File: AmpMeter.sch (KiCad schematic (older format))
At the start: 49 parts, among them J1 Vin L1-L3, J2 Serial, J3 ct1, J4 ct2, J5 ct3, J6 ct L1-L3, T1 Transformer_1P_1S, T2 Transformer_1P_1S, T3 Transformer_1P_1S, U1 LTV-817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

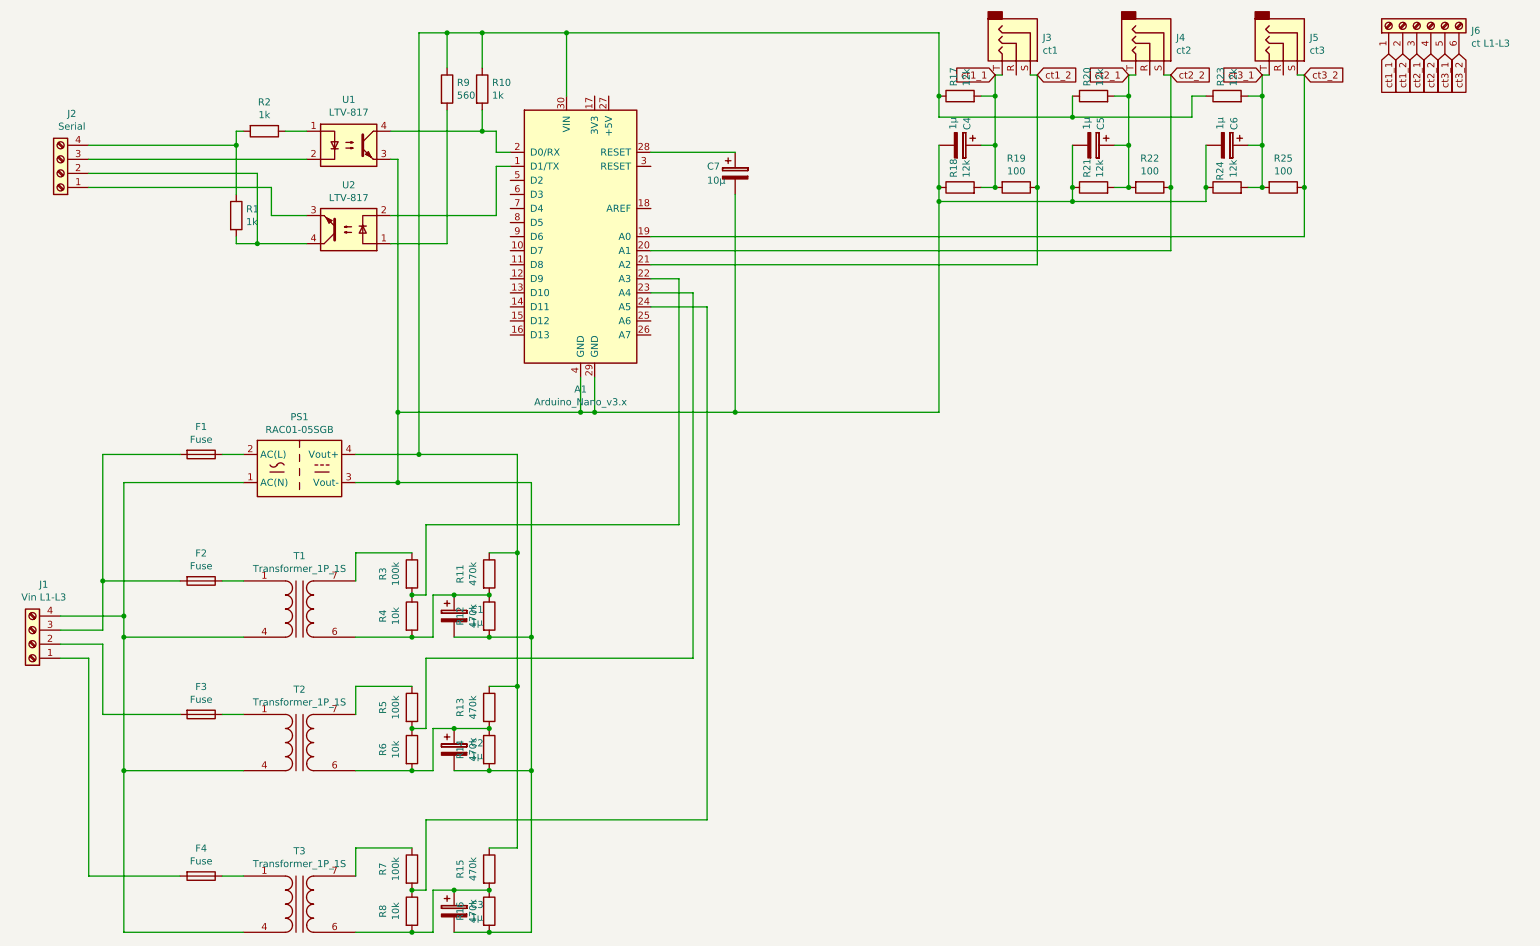
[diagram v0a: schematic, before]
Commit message: change values on parts
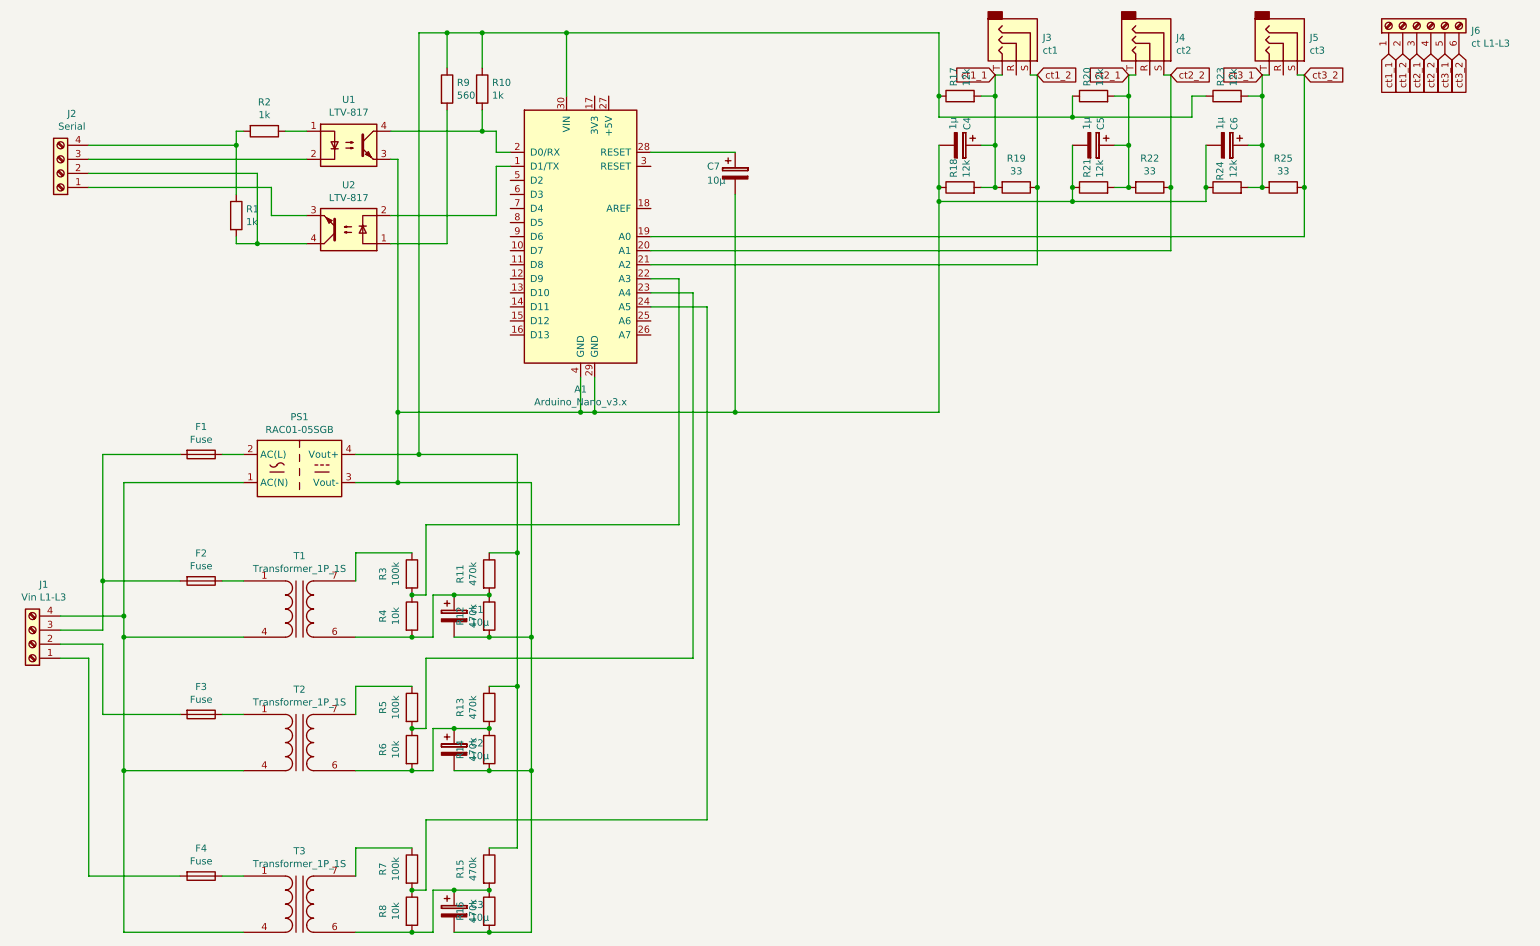
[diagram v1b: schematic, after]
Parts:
- C1, C2, C3: value 1µ -> 10µ
- R19, R22, R25: value 100 -> 33
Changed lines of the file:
@@
 P 7650 1950
 F 0 "R19" V 7443 1950 50  0000 C CNN
-F 1 "100" V 7534 1950 50  0000 C CNN
+F 1 "33" V 7534 1950 50  0000 C CNN
 F 2 "Resistor_SMD:R_1206_3216Metric" V 7580 1950 50  0001 C CNN
 F 3 "~" H 7650 1950 50  0001 C CNN
@@
 P 8600 1950
 F 0 "R22" V 8393 1950 50  0000 C CNN
-F 1 "100" V 8484 1950 50  0000 C CNN
+F 1 "33" V 8484 1950 50  0000 C CNN
 F 2 "Resistor_SMD:R_1206_3216Metric" V 8530 1950 50  0001 C CNN
 F 3 "~" H 8600 1950 50  0001 C CNN
@@
 P 9550 1950
 F 0 "R25" V 9343 1950 50  0000 C CNN
-F 1 "100" V 9434 1950 50  0000 C CNN
+F 1 "33" V 9434 1950 50  0000 C CNN
 F 2 "Resistor_SMD:R_1206_3216Metric" V 9480 1950 50  0001 C CNN
 F 3 "~" H 9550 1950 50  0001 C CNN
@@
 P 3650 5000
 F 0 "C1" H 3768 5046 50  0000 L CNN
-F 1 "1µ" H 3768 4955 50  0000 L CNN
+F 1 "10µ" H 3768 4955 50  0000 L CNN
 F 2 "Capacitor_THT:CP_Radial_D8.0mm_P5.00mm" H 3688 4850 50  0001 C CNN
 F 3 "~" H 3650 5000 50  0001 C CNN
@@
 P 3650 5950
 F 0 "C2" H 3768 5996 50  0000 L CNN
-F 1 "1µ" H 3768 5905 50  0000 L CNN
+F 1 "10µ" H 3768 5905 50  0000 L CNN
 F 2 "Capacitor_THT:CP_Radial_D8.0mm_P5.00mm" H 3688 5800 50  0001 C CNN
 F 3 "~" H 3650 5950 50  0001 C CNN
@@
 P 3650 7100
 F 0 "C3" H 3768 7146 50  0000 L CNN
-F 1 "1µ" H 3768 7055 50  0000 L CNN
+F 1 "10µ" H 3768 7055 50  0000 L CNN
 F 2 "Capacitor_THT:CP_Radial_D8.0mm_P5.00mm" H 3688 6950 50  0001 C CNN
 F 3 "~" H 3650 7100 50  0001 C CNN
